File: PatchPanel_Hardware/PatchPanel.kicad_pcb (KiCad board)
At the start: 2 copper layers, 194.3 x 97.2 mm, 87 parts, among them Q1 Q_PMOS_DGS, Q10 Q_PMOS_DGS, Q11 Q_NMOS_DGS, Q12 Q_NMOS_DGS, Q13 Q_PMOS_DGS, Q14 Q_PMOS_DGS, Q15 Q_NMOS_DGS, Q16 Q_NMOS_DGS, Q17 Q_PMOS_DGS, Q18 Q_PMOS_DGS, Q19 Q_NMOS_DGS, Q2 Q_PMOS_DGS, Q20 Q_NMOS_DGS, Q21 Q_PMOS_DGS, Q22 Q_PMOS_DGS, Q23 Q_NMOS_DGS, Q24 Q_NMOS_DGS, Q25 Q_PMOS_DGS, Q26 Q_PMOS_DGS, Q27 Q_NMOS_DGS, Q28 Q_NMOS_DGS, Q29 Q_PMOS_DGS, Q3 Q_NMOS_DGS, Q30 Q_PMOS_DGS, Q31 Q_NMOS_DGS, Q32 Q_NMOS_DGS, Q4 Q_NMOS_DGS, Q5 Q_PMOS_DGS, Q6 Q_PMOS_DGS, Q7 Q_NMOS_DGS, Q8 Q_NMOS_DGS, Q9 Q_PMOS_DGS

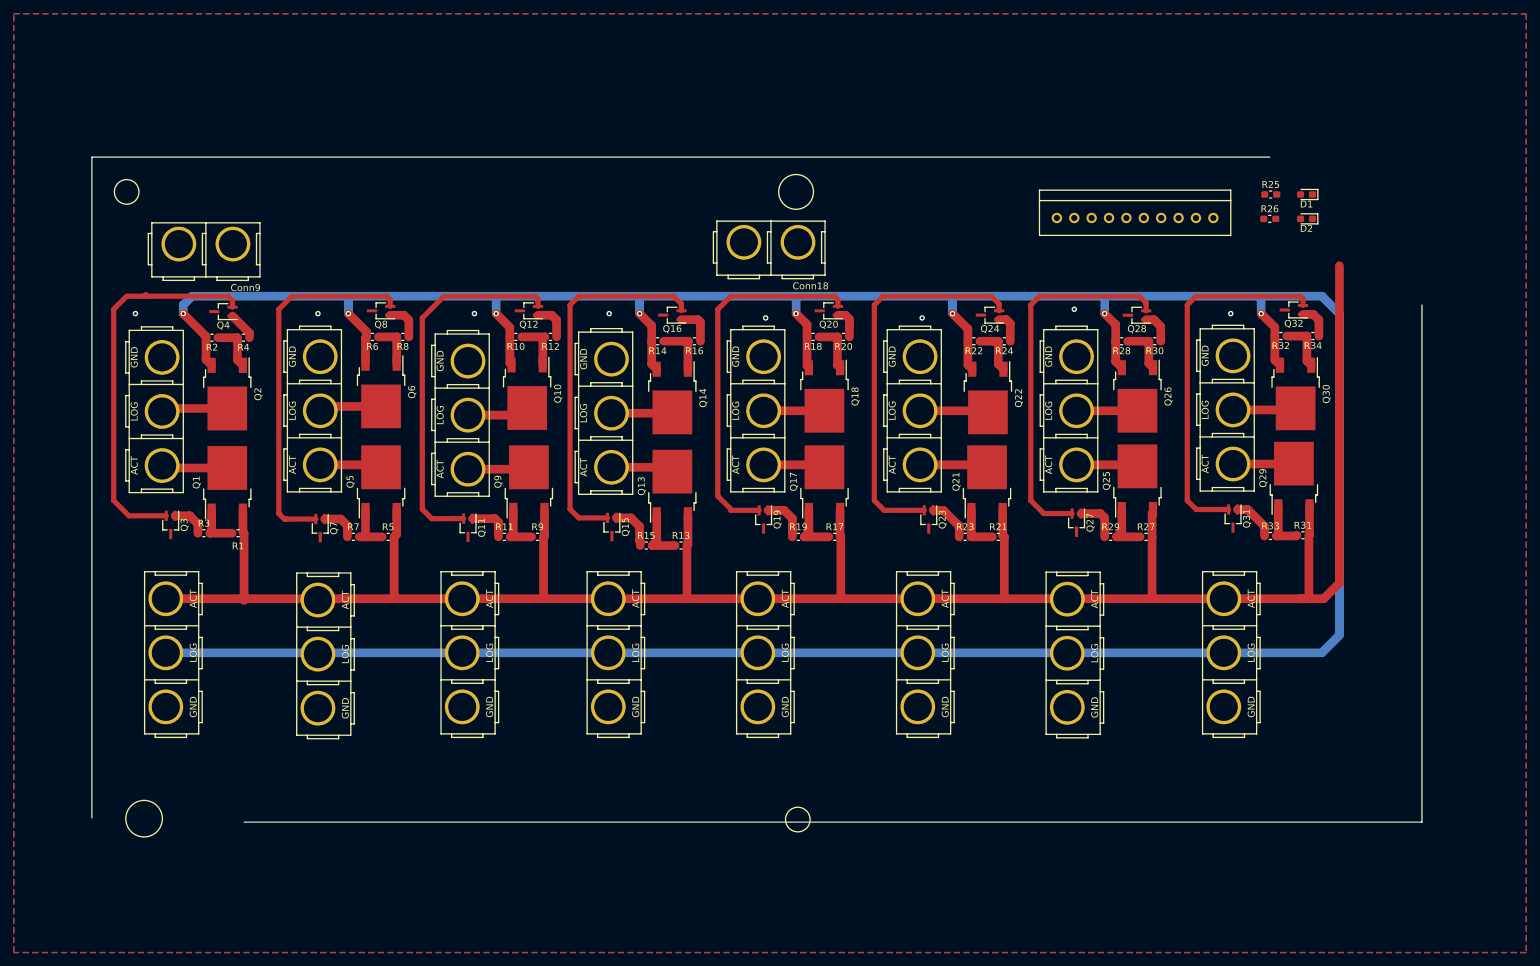
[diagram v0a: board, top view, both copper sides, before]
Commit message: change molex
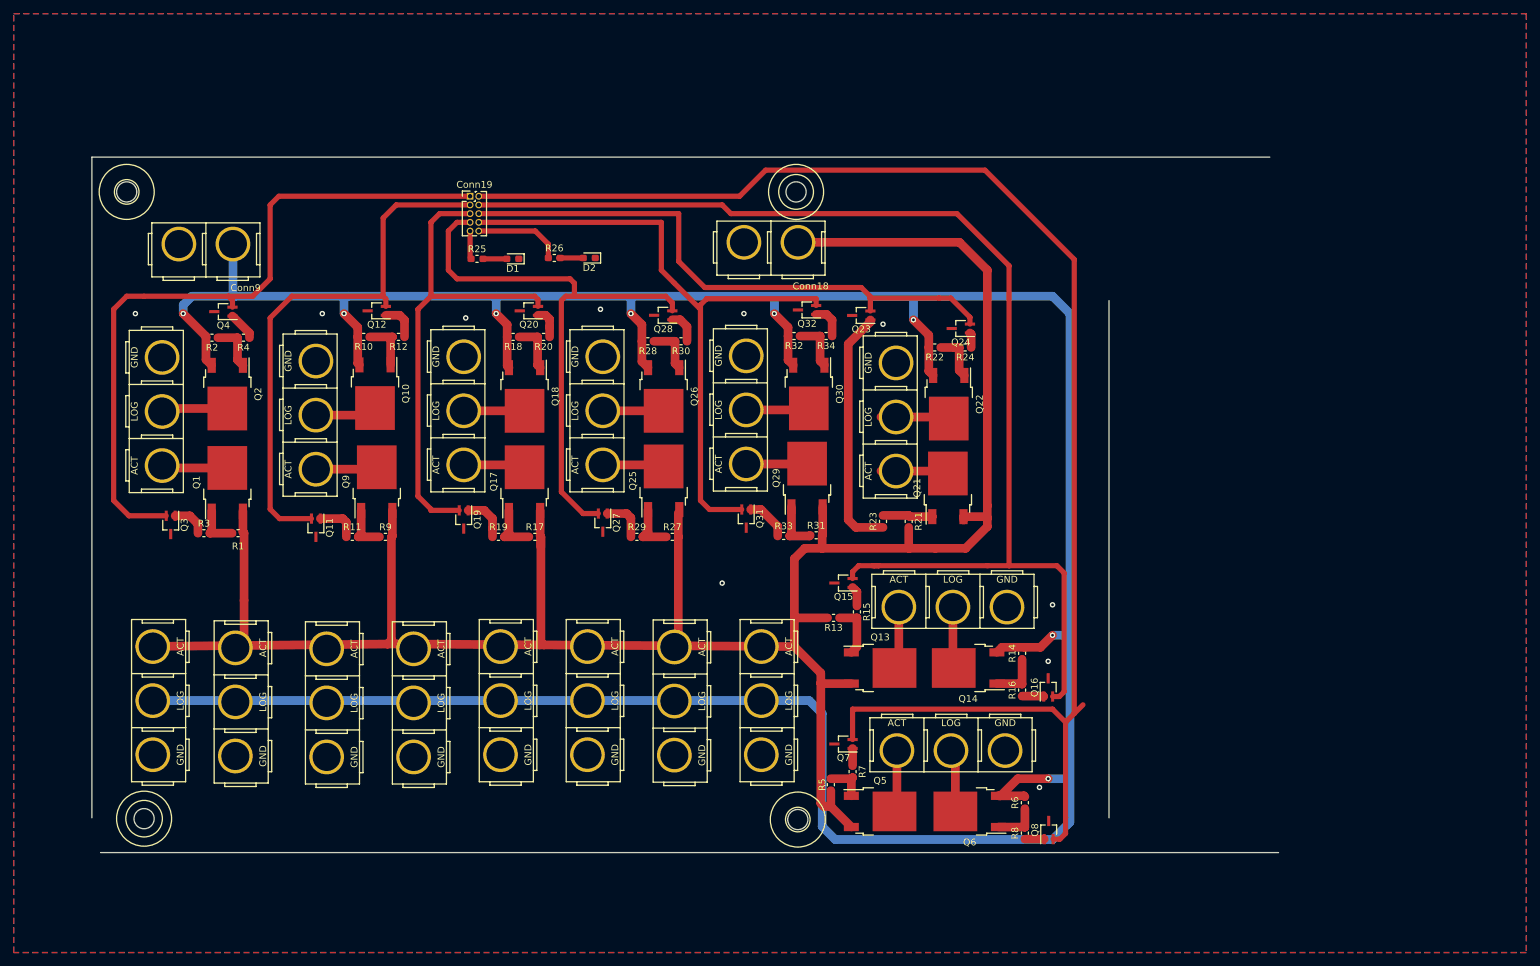
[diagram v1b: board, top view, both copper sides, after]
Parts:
- added REF**: 4_40_Hole, MRDT_Drill_Holes:4_40_Hole, F.Cu at (49.5, 142.4)
- added REF**: 4_40_Hole, MRDT_Drill_Holes:4_40_Hole, F.Cu at (145.0, 142.5)
- added REF**: 4_40_Hole, MRDT_Drill_Holes:4_40_Hole, F.Cu at (47.0, 50.8)
- added REF**: 4_40_Hole, MRDT_Drill_Holes:4_40_Hole, F.Cu at (144.8, 50.8)
- Conn19: footprint MRDT_Connectors:MOLEX_SL_10_Vertical -> Connector_PinHeader_1.27mm:PinHeader_2x05_P1.27mm_Vertical
- moved Q8 123.6 mm to (181.7, 144.0), turned to 90 degrees
- moved Conn2 122.7 mm to (179.3, 127.6), turned to 180 degrees
- moved R6 117.1 mm to (178.2, 140.0), turned to 90 degrees
- moved R25 116.3 mm to (98.2, 60.6)
- moved D1 116.3 mm to (103.4, 60.6)
- moved R8 116.3 mm to (178.2, 144.5), turned to 90 degrees
- moved Q6 105.6 mm to (170.1, 141.3), turned to 180 degrees
- moved D2 104.9 mm to (114.6, 60.5)
- moved R26 104.7 mm to (109.5, 60.5)
- moved Conn19 97.2 mm to (97.2, 51.4)
- moved Q5 87.4 mm to (157.1, 141.3), turned to 0 degrees
- moved Q7 82.7 mm to (151.7, 131.5), turned to 180 degrees
- moved R7 80.6 mm to (153.0, 135.5), turned to 270 degrees
- moved Q16 77.3 mm to (181.6, 123.2), turned to 90 degrees
- moved Conn4 75.4 mm to (179.5, 106.7), turned to 180 degrees
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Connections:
- Q16 pad 3: Net-(Q16-Pad3) -> GND
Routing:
- net /PL2: track 53.8 -> 218.7 mm
- net /PL0: track 54.1 -> 177.8 mm
- net /PL3: track 56.3 -> 103.6 mm
- net /PF3: track 53.7 -> 95.2 mm
- net Net-(Q23-Pad1): track 6.32 -> 36.1 mm
- net /PG0: track 54.3 -> 83.2 mm
- net /PL4: track 56.7 -> 85.3 mm
- net /PL1: track 54.0 -> 78.9 mm
- net /Vact: track 321.6 -> 341.9 mm
- net /PL5: track 53.8 -> 70.9 mm
- net /Vlog: track 479.9 -> 463.2 mm
- net /PF1: track 0.00 -> 13.0 mm
- net /PF2: track 0.00 -> 3.81 mm
- net Net-(Q15-Pad1): track 6.73 -> 2.96 mm
- net Net-(D2-Pad2): track 0.00 -> 3.61 mm
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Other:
- board size 194.3 x 97.2 mm -> 173.4 x 101.6 mm

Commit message: add LED to anderson
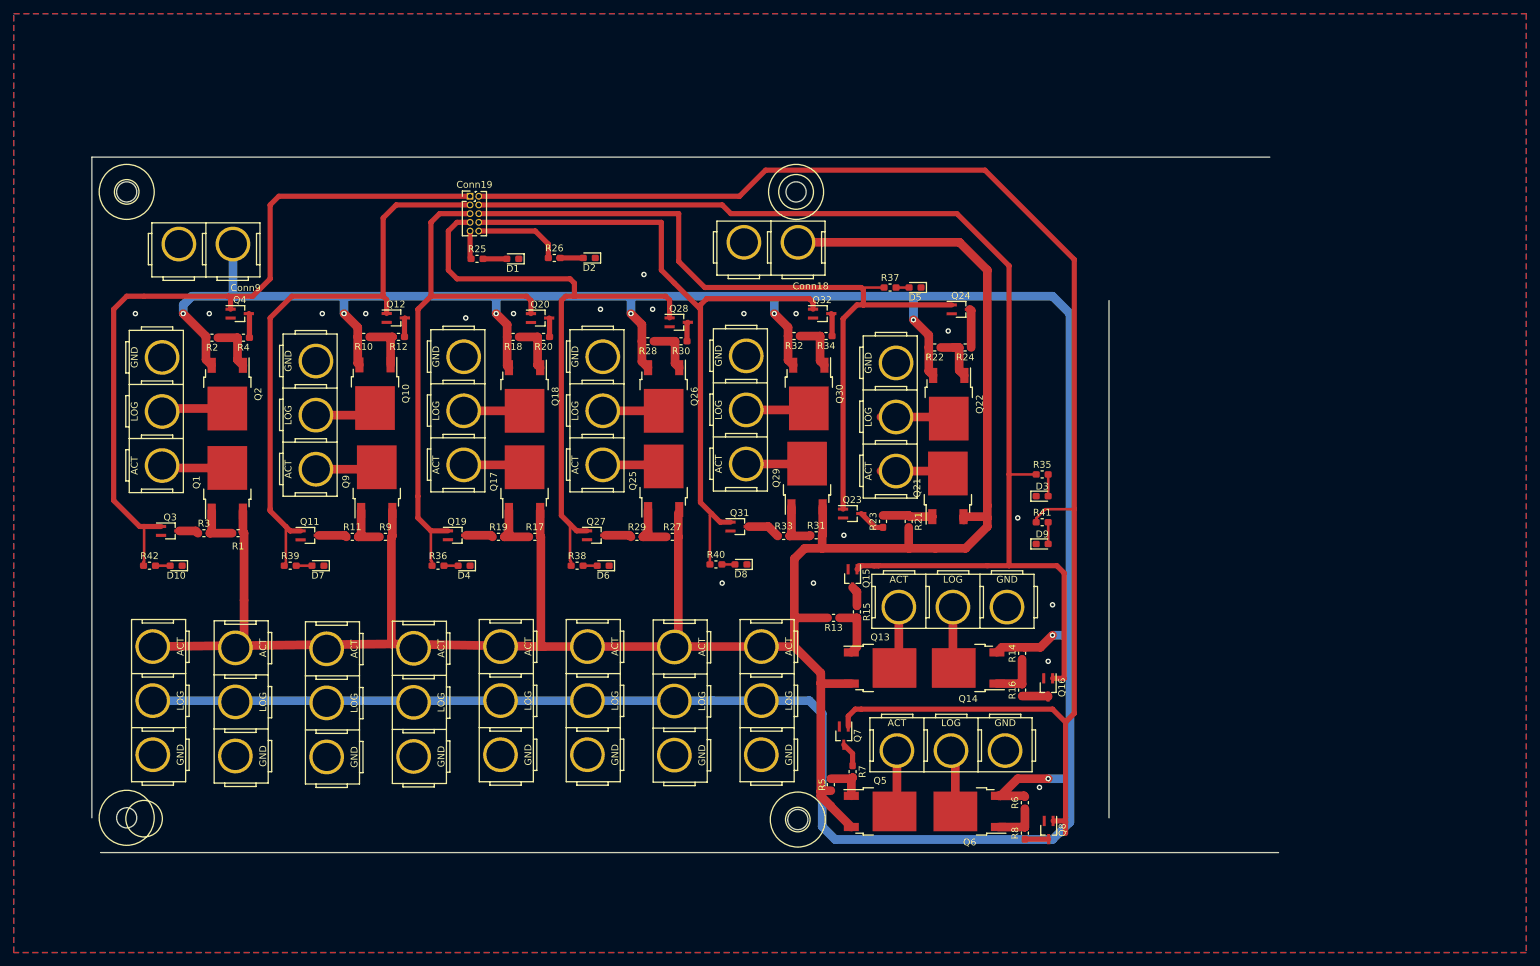
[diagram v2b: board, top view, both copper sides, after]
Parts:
- added D10: OrangeLED, LED_SMD:LED_0603_1608Metric_Pad1.05x0.95mm_HandSolder, F.Cu at (54.2, 105.4)
- added D3: OrangeLED, LED_SMD:LED_0603_1608Metric_Pad1.05x0.95mm_HandSolder, F.Cu at (180.7, 95.2)
- added D4: OrangeLED, LED_SMD:LED_0603_1608Metric_Pad1.05x0.95mm_HandSolder, F.Cu at (96.3, 105.4)
- added D5: OrangeLED, LED_SMD:LED_0603_1608Metric_Pad1.05x0.95mm_HandSolder, F.Cu at (162.2, 64.8)
- added D6: OrangeLED, LED_SMD:LED_0603_1608Metric_Pad1.05x0.95mm_HandSolder, F.Cu at (116.6, 105.4)
- added D7: OrangeLED, LED_SMD:LED_0603_1608Metric_Pad1.05x0.95mm_HandSolder, F.Cu at (74.9, 105.4)
- added D8: OrangeLED, LED_SMD:LED_0603_1608Metric_Pad1.05x0.95mm_HandSolder, F.Cu at (136.7, 105.2)
- added D9: OrangeLED, LED_SMD:LED_0603_1608Metric_Pad1.05x0.95mm_HandSolder, F.Cu at (180.7, 102.2)
- added R35: 300, Resistor_SMD:R_0603_1608Metric_Pad1.05x0.95mm_HandSolder, F.Cu at (180.7, 92.1)
- added R36: 300, Resistor_SMD:R_0603_1608Metric_Pad1.05x0.95mm_HandSolder, F.Cu at (92.5, 105.4)
- added R37: 300, Resistor_SMD:R_0603_1608Metric_Pad1.05x0.95mm_HandSolder, F.Cu at (158.5, 64.8)
- added R38: 300, Resistor_SMD:R_0603_1608Metric_Pad1.05x0.95mm_HandSolder, F.Cu at (112.8, 105.4)
- added R39: 300, Resistor_SMD:R_0603_1608Metric_Pad1.05x0.95mm_HandSolder, F.Cu at (70.9, 105.4)
- added R40: 300, Resistor_SMD:R_0603_1608Metric_Pad1.05x0.95mm_HandSolder, F.Cu at (133.1, 105.2)
- added R41: 300, Resistor_SMD:R_0603_1608Metric_Pad1.05x0.95mm_HandSolder, F.Cu at (180.7, 99.1)
- added R42: 300, Resistor_SMD:R_0603_1608Metric_Pad1.05x0.95mm_HandSolder, F.Cu at (50.3, 105.4)
- Q1, Q10, Q13, Q14, Q17, Q18, Q2, Q21, Q22, Q25, Q26, Q29, Q30, Q5, Q6, Q9: value Q_PMOS_DGS -> Q_PMOS_GDS
- Q11, Q12, Q15, Q16, Q19, Q20, Q23, Q24, Q27, Q28, Q3, Q31, Q32, Q4, Q7, Q8: value Q_NMOS_DGS -> Q_NMOS_GSD
- R25, R26: value R -> 300
- moved Q23 29.0 mm to (153.0, 97.8), turned to 0 degrees
- moved Q12 2.97 mm to (86.3, 69.2), turned to 0 degrees
- moved Q24 2.80 mm to (168.8, 68.0), turned to 0 degrees
- moved REF** 2.54 mm to (47.0, 142.2)
- moved Q19 2.51 mm to (95.2, 101.0), turned to 0 degrees
- moved Q28 2.49 mm to (127.6, 69.8), turned to 0 degrees
- moved Q4 2.40 mm to (63.5, 68.6), turned to 0 degrees
- moved Q32 2.27 mm to (148.6, 68.6), turned to 0 degrees
- moved Q27 2.08 mm to (115.6, 101.0), turned to 0 degrees
- moved Q20 1.94 mm to (107.4, 69.2), turned to 0 degrees
- moved Q31 1.52 mm to (136.5, 99.7), turned to 0 degrees
- moved Q15 1.49 mm to (153.0, 107.3), turned to 270 degrees
- moved Q11 1.44 mm to (73.7, 101.0), turned to 0 degrees
- moved Q7 1.23 mm to (151.8, 130.2), turned to 270 degrees
- moved Q3 0.88 mm to (53.3, 100.3), turned to 0 degrees
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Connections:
- net /PF1 renamed Net-(Conn19-Pad10)
- net /PF2 renamed Net-(Conn19-Pad9)
- Q11 pad 1: Net-(Q11-Pad1) -> /PL1
- Q11 pad 2: /PL1 -> GND
- Q11 pad 3: GND -> Net-(Q11-Pad3)
- Q12 pad 1: Net-(Q12-Pad1) -> /PL1
- Q12 pad 2: /PL1 -> GND
- Q12 pad 3: GND -> Net-(Q12-Pad3)
- Q15 pad 1: Net-(Q15-Pad1) -> /PL0
- Q15 pad 2: /PL0 -> GND
- Q15 pad 3: GND -> Net-(Q15-Pad3)
- Q16 pad 1: Net-(Q16-Pad1) -> /PL0
- Q16 pad 2: /PL0 -> GND
- Q16 pad 3: GND -> Net-(Q16-Pad3)
- Q19 pad 1: Net-(Q19-Pad1) -> /PL5
- Q19 pad 2: /PL5 -> GND
- Q19 pad 3: GND -> Net-(Q19-Pad3)
- Q20 pad 1: Net-(Q20-Pad1) -> /PL5
- Q20 pad 2: /PL5 -> GND
- Q20 pad 3: GND -> Net-(Q20-Pad3)
- Q23 pad 1: Net-(Q23-Pad1) -> /PL4
- Q23 pad 2: /PL4 -> GND
- Q23 pad 3: GND -> Net-(Q23-Pad3)
- Q24 pad 1: Net-(Q24-Pad1) -> /PL4
- Q24 pad 2: /PL4 -> GND
- Q24 pad 3: GND -> Net-(Q24-Pad3)
- Q27 pad 1: Net-(Q27-Pad1) -> /PG0
- Q27 pad 2: /PG0 -> GND
- Q27 pad 3: GND -> Net-(Q27-Pad3)
- Q28 pad 1: Net-(Q28-Pad1) -> /PG0
- Q28 pad 2: /PG0 -> GND
- Q28 pad 3: GND -> Net-(Q28-Pad3)
- Q3 pad 1: Net-(Q3-Pad1) -> /PL3
- Q3 pad 2: /PL3 -> GND
- Q3 pad 3: GND -> Net-(Q3-Pad3)
- Q31 pad 1: Net-(Q31-Pad1) -> /PF3
- Q31 pad 2: /PF3 -> GND
- Q31 pad 3: GND -> Net-(Q31-Pad3)
- Q32 pad 1: Net-(Q32-Pad1) -> /PF3
- Q32 pad 2: /PF3 -> GND
- Q32 pad 3: GND -> Net-(Q32-Pad3)
- Q4 pad 1: Net-(Q4-Pad1) -> /PL3
- Q4 pad 2: /PL3 -> GND
- Q4 pad 3: GND -> Net-(Q4-Pad3)
- Q7 pad 1: Net-(Q7-Pad1) -> /PL2
- Q7 pad 2: /PL2 -> GND
- Q7 pad 3: GND -> Net-(Q7-Pad3)
- Q8 pad 1: Net-(Q8-Pad1) -> /PL2
- Q8 pad 2: /PL2 -> GND
- Q8 pad 3: GND -> Net-(Q8-Pad3)
- R11 pad 1: Net-(Q11-Pad1) -> Net-(Q11-Pad3)
- R12 pad 1: Net-(Q12-Pad1) -> Net-(Q12-Pad3)
- R15 pad 1: Net-(Q15-Pad1) -> Net-(Q15-Pad3)
- R16 pad 1: Net-(Q16-Pad1) -> Net-(Q16-Pad3)
- R19 pad 1: Net-(Q19-Pad1) -> Net-(Q19-Pad3)
- R20 pad 1: Net-(Q20-Pad1) -> Net-(Q20-Pad3)
- R23 pad 1: Net-(Q23-Pad1) -> Net-(Q23-Pad3)
- R24 pad 1: Net-(Q24-Pad1) -> Net-(Q24-Pad3)
- R29 pad 1: Net-(Q27-Pad1) -> Net-(Q27-Pad3)
- R3 pad 1: Net-(Q3-Pad1) -> Net-(Q3-Pad3)
- R30 pad 1: Net-(Q28-Pad1) -> Net-(Q28-Pad3)
- R33 pad 1: Net-(Q31-Pad1) -> Net-(Q31-Pad3)
- R34 pad 1: Net-(Q32-Pad1) -> Net-(Q32-Pad3)
- R4 pad 1: Net-(Q4-Pad1) -> Net-(Q4-Pad3)
- R7 pad 1: Net-(Q7-Pad1) -> Net-(Q7-Pad3)
- R8 pad 1: Net-(Q8-Pad1) -> Net-(Q8-Pad3)
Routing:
- net Net-(Q23-Pad1): track 36.1 -> 0.00 mm
- net /PL4: track 85.3 -> 115.0 mm
- net /PG0: track 83.2 -> 91.6 mm
- net Net-(Q19-Pad1): track 6.72 -> 0.00 mm
- net /PF3: track 95.2 -> 101.7 mm
- net Net-(Q27-Pad1): track 6.49 -> 0.00 mm
- net /PL5: track 70.9 -> 77.3 mm
- net Net-(Q31-Pad1): track 6.38 -> 0.00 mm
- net /PL1: track 78.9 -> 85.2 mm
- net Net-(Q11-Pad1): track 6.15 -> 0.00 mm
- net /PL3: track 103.6 -> 109.5 mm
- net Net-(Q24-Pad3): track 0.00 -> 5.64 mm
- net Net-(Q12-Pad1): track 5.47 -> 0.00 mm
- net Net-(Q3-Pad1): track 5.17 -> 0.00 mm
- net Net-(Q32-Pad1): track 5.01 -> 0.00 mm
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
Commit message: BoardReview
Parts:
- removed D1, D2: LED, LED_SMD:LED_0603_1608Metric_Pad1.05x0.95mm_HandSolder
- removed R25, R26: 300, Resistor_SMD:R_0603_1608Metric_Pad1.05x0.95mm_HandSolder
- removed the REF** at (47.0, 142.2)
- removed the REF** at (145.0, 142.5)
- added REF**: 4_40_Hole, MRDT_Drill_Holes:4_40_Hole, F.Cu at (46.8, 142.4)
- added REF**: 4_40_Hole, MRDT_Drill_Holes:4_40_Hole, F.Cu at (144.8, 142.5)
- moved R41 41.9 mm to (188.2, 140.3), turned to 180 degrees
- moved D9 38.2 mm to (183.9, 140.3)
- moved R35 16.9 mm to (186.4, 108.0)
- moved D3 16.3 mm to (186.4, 110.5)
- moved R13 8.38 mm to (148.8, 121.3)
- moved Q15 7.75 mm to (148.6, 113.6)
- moved R15 7.67 mm to (148.8, 118.1), turned to 0 degrees
- moved Conn11 1.27 mm to (145.8, 137.0)
- moved Conn14 1.27 mm to (120.4, 137.0)
- moved Conn10 1.27 mm to (82.3, 137.3)
- moved Conn12 1.27 mm to (95.0, 137.2)
- moved Conn13 1.27 mm to (107.7, 137.0)
- moved Conn15 1.27 mm to (56.9, 137.0)
- moved Conn17 1.27 mm to (68.9, 137.2)
- moved Conn16 1.27 mm to (133.1, 137.0)
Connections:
- net /PF3 renamed PB8
- net /PG0 renamed PB7
- net /PL0 renamed PB4
- net /PL1 renamed PB3
- net /PL2 renamed PB2
- net /PL3 renamed PB1
- net /PL4 renamed PB6
- net /PL5 renamed PB5
- Conn19 pad 10: Net-(Conn19-Pad10) -> GND
- Conn19 pad 9: Net-(Conn19-Pad9) -> GND
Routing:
- net /Vact: track 337.5 -> 0.55 mm
- net GND: track 0.00 -> 56.5 mm, vias 19 -> 29
- net PB4: track 178.2 -> 198.1 mm
- net /Vlog: track 463.2 -> 480.6 mm
- net Net-(Conn19-Pad10): track 13.0 -> 0.00 mm
- net PB2: track 221.4 -> 231.3 mm
- net Net-(Conn19-Pad9): track 3.81 -> 0.00 mm
- net Net-(D2-Pad2): track 3.61 -> 0.00 mm
- net Net-(D1-Pad2): track 3.47 -> 0.00 mm
- net Net-(Q13-Pad1): track 7.92 -> 6.41 mm
- net Net-(D9-Pad2): track 3.17 -> 2.54 mm
- net Net-(D3-Pad2): track 3.17 -> 2.54 mm
- added copper zone on F.Cu, net /Vact
- removed copper zone on F.Cu, net GND
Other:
- board size 173.4 x 101.6 mm -> 148.6 x 101.6 mm
- board text added: "PB1"
- board text added: "PB2"
- board text added: "PB3"
- board text added: "PB4"
- board text added: "PB5"
- board text added: "PB6"
- board text added: "PB7"
- board text added: "PB8"
